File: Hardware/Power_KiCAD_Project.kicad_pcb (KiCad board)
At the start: 4 copper layers, 80 x 93.2 mm, 83 parts, among them J1 Barrel_Jack_MountingPin, J2 XT60 Cell 5, J3 XT60 Cell 4, J4 XT60 Cell 3, J5 XT60 Cell 2, J6 XT60 Cell 1, J7 XT60 To External Switch, J8 L717SDC37P1ACH4F, Q1 PSMN2R6-40YS, Q2 BSS84PH6327XTSA2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

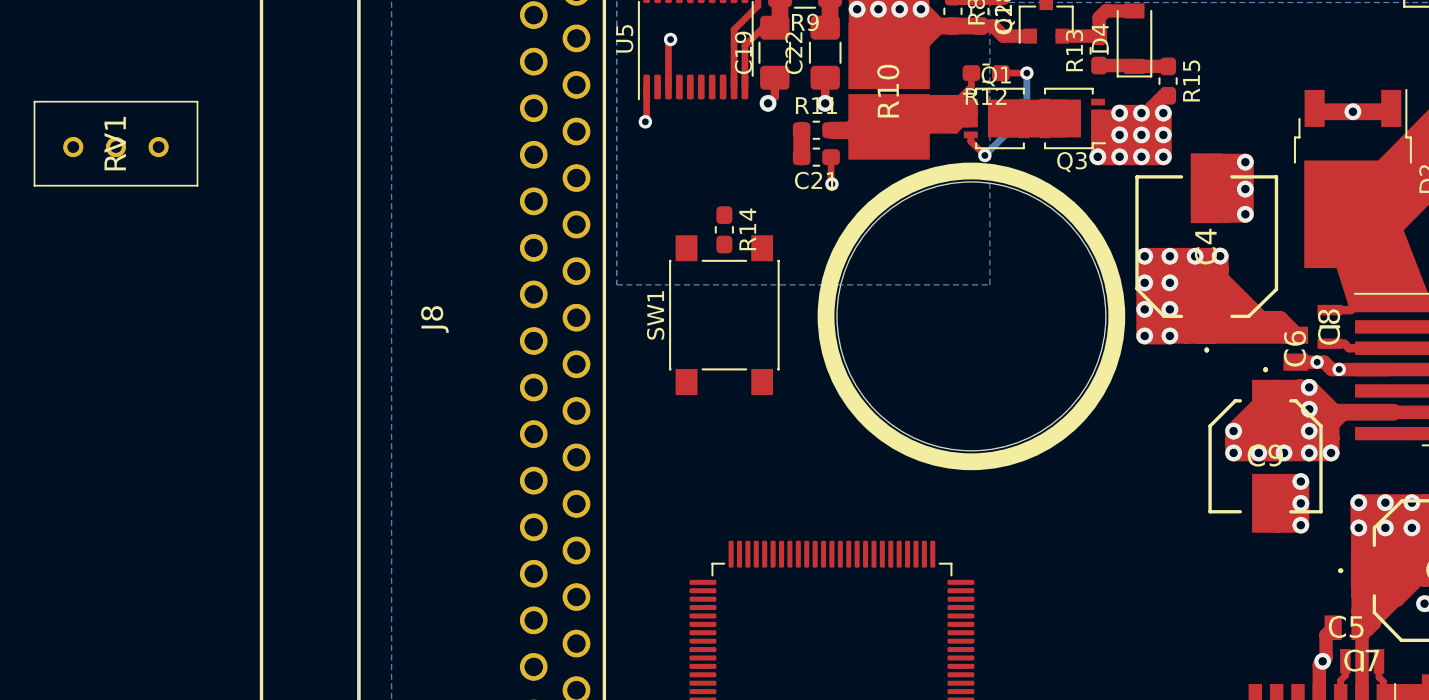
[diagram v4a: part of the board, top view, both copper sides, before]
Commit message: Attempting to add ground vias to help with emi
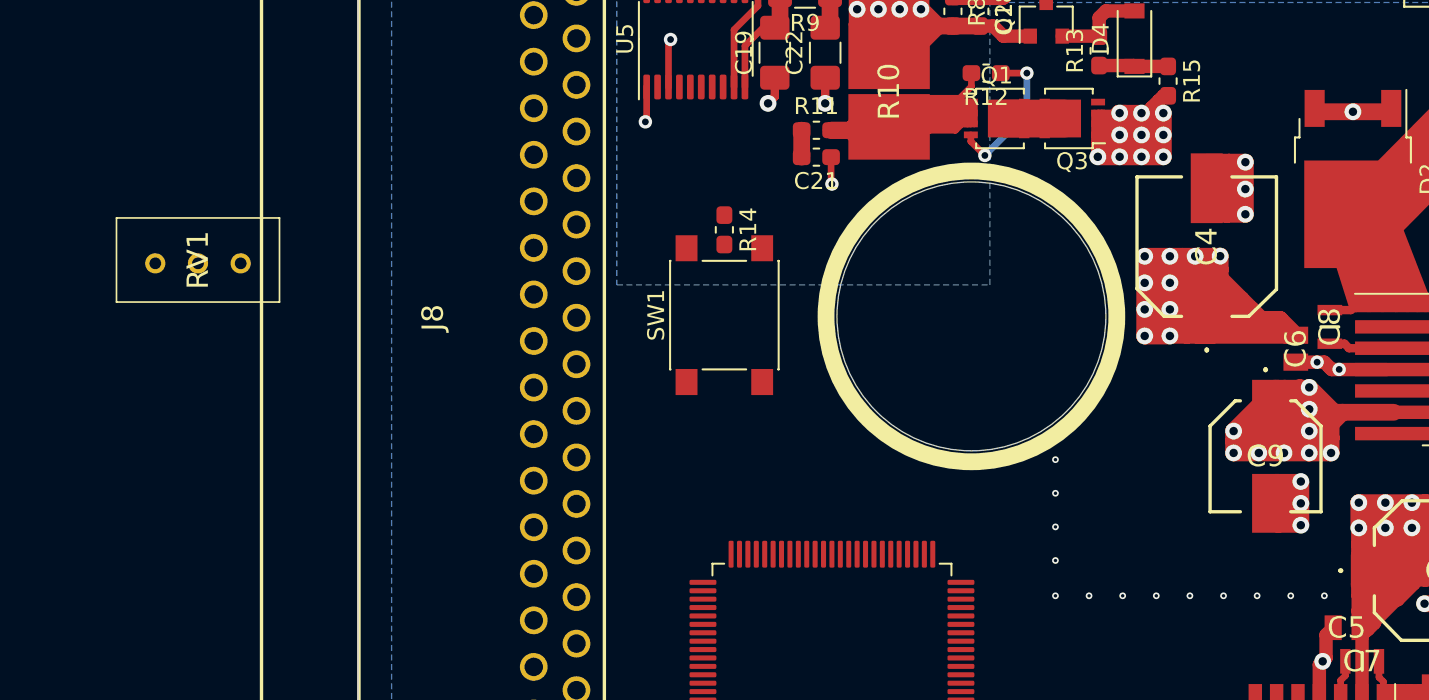
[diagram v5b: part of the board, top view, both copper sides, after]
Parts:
- moved RV1 8.47 mm to (70.5, 95.1)
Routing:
- net GND: vias 27 -> 65
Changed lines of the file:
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@@
     (thickness 1.6)
     (drawings 27)
-    (tracks 794)
+    (tracks 832)
     (zones 0)
     (modules 83)
@@
     (aux_axis_origin 80 145)
     (grid_origin 80 145)
-    (visible_elements 7FFDF77F)
+    (visible_elements 7FFDFF7F)
     (pcbplotparams
       (layerselection 0x010fc_ffffffff)
@@
   )
   (module RDT_Custom_Footprints:T93YA5K10 (layer F.Cu)
-    (at 65.6 88.2 270)
+    (at 70.48 95.12 270)
     (descr T93YA)
     (tags "Variable Resistor")
@@
   (segment (start 148.69 115.57) (end 149.66 114.6) (width 1) (layer F.Cu) (net 2))
   (segment (start 146.56 115.57) (end 148.69 115.57) (width 1) (layer F.Cu) (net 2))
+  (via (at 121.5 115.1) (size 0.4) (drill 0.2) (layers F.Cu B.Cu) (net 2))
+  (via (at 123.5 115.1) (size 0.4) (drill 0.2) (layers F.Cu B.Cu) (net 2))
+  (via (at 125.5 115.1) (size 0.4) (drill 0.2) (layers F.Cu B.Cu) (net 2))
+  (via (at 127.5 115.1) (size 0.4) (drill 0.2) (layers F.Cu B.Cu) (net 2))
+  (via (at 129.5 115.1) (size 0.4) (drill 0.2) (layers F.Cu B.Cu) (net 2))
+  (via (at 131.5 115.1) (size 0.4) (drill 0.2) (layers F.Cu B.Cu) (net 2))
+  (via (at 133.5 115.1) (size 0.4) (drill 0.2) (layers F.Cu B.Cu) (net 2))
+  (via (at 135.5 115.1) (size 0.4) (drill 0.2) (layers F.Cu B.Cu) (net 2))
+  (via (at 137.5 115.1) (size 0.4) (drill 0.2) (layers F.Cu B.Cu) (net 2))
+  (via (at 121.5 113) (size 0.4) (drill 0.2) (layers F.Cu B.Cu) (net 2))
+  (via (at 121.5 111) (size 0.4) (drill 0.2) (layers F.Cu B.Cu) (net 2))
+  (via (at 121.5 109) (size 0.4) (drill 0.2) (layers F.Cu B.Cu) (net 2))
+  (via (at 121.5 107) (size 0.4) (drill 0.2) (layers F.Cu B.Cu) (net 2))
+  (via (at 116.5 107.22) (size 0.4) (drill 0.2) (layers F.Cu B.Cu) (net 2))
+  (via (at 118.67355 106.945417) (size 0.4) (drill 0.2) (layers F.Cu B.Cu) (net 2))
+  (via (at 120.710527 106.13892) (size 0.4) (drill 0.2) (layers F.Cu B.Cu) (net 2))
+  (via (at 122.482942 104.851186) (size 0.4) (drill 0.2) (layers F.Cu B.Cu) (net 2))
+  (via (at 123.879426 103.163126) (size 0.4) (drill 0.2) (layers F.Cu B.Cu) (net 2))
+  (via (at 124.812234 101.180809) (size 0.4) (drill 0.2) (layers F.Cu B.Cu) (net 2))
+  (via (at 125.222754 99.028789) (size 0.4) (drill 0.2) (layers F.Cu B.Cu) (net 2))
+  (via (at 125.085191 96.842287) (size 0.4) (drill 0.2) (layers F.Cu B.Cu) (net 2))
+  (via (at 124.408188 94.758689) (size 0.4) (drill 0.2) (layers F.Cu B.Cu) (net 2))
+  (via (at 123.234286 92.908914) (size 0.4) (drill 0.2) (layers F.Cu B.Cu) (net 2))
+  (via (at 121.637243 91.409191) (size 0.4) (drill 0.2) (layers F.Cu B.Cu) (net 2))
+  (via (at 119.717409 90.353754) (size 0.4) (drill 0.2) (layers F.Cu B.Cu) (net 2))
+  (via (at 117.595412 89.808918) (size 0.4) (drill 0.2) (layers F.Cu B.Cu) (net 2))
+  (via (at 115.404588 89.808918) (size 0.4) (drill 0.2) (layers F.Cu B.Cu) (net 2))
+  (via (at 113.282591 90.353754) (size 0.4) (drill 0.2) (layers F.Cu B.Cu) (net 2))
+  (via (at 111.362757 91.409191) (size 0.4) (drill 0.2) (layers F.Cu B.Cu) (net 2))
+  (via (at 109.765714 92.908914) (size 0.4) (drill 0.2) (layers F.Cu B.Cu) (net 2))
+  (via (at 108.591812 94.758689) (size 0.4) (drill 0.2) (layers F.Cu B.Cu) (net 2))
+  (via (at 107.914809 96.842287) (size 0.4) (drill 0.2) (layers F.Cu B.Cu) (net 2))
+  (via (at 107.777246 99.028789) (size 0.4) (drill 0.2) (layers F.Cu B.Cu) (net 2))
+  (via (at 108.187766 101.180809) (size 0.4) (drill 0.2) (layers F.Cu B.Cu) (net 2))
+  (via (at 109.120574 103.163126) (size 0.4) (drill 0.2) (layers F.Cu B.Cu) (net 2))
+  (via (at 110.517058 104.851186) (size 0.4) (drill 0.2) (layers F.Cu B.Cu) (net 2))
+  (via (at 112.289473 106.13892) (size 0.4) (drill 0.2) (layers F.Cu B.Cu) (net 2))
+  (via (at 114.32645 106.945417) (size 0.4) (drill 0.2) (layers F.Cu B.Cu) (net 2))
   (segment (start 134.42 103.58) (end 134 104) (width 0.8) (layer F.Cu) (net 3))
   (segment (start 136.12 103.98) (end 136.1 104) (width 0.8) (layer F.Cu) (net 3))
@@
     (polygon
       (pts
-        (xy 158 126.5) (xy 94.7 126.45) (xy 94.7 103.3) (xy 121 103.3) (xy 121 115.6)
+        (xy 158 126.5) (xy 94.7 126.45) (xy 94.7 103.5) (xy 121 103.5) (xy 121 115.6)
         (xy 146.9 115.6) (xy 146.9 108) (xy 131.3 108) (xy 131.3 104.1) (xy 132.6 104.1)
         (xy 132.6 102.1) (xy 143.8 102) (xy 143.8 88.5) (xy 158 88.5)

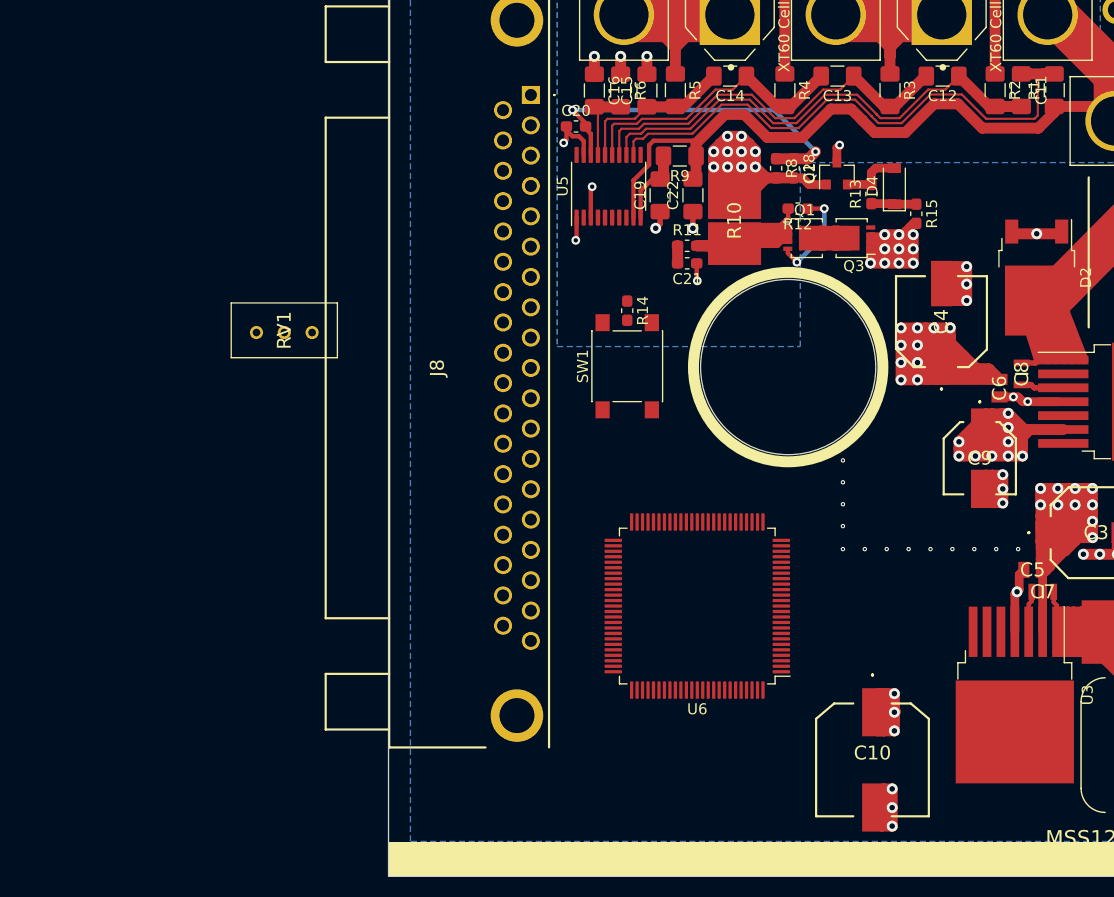
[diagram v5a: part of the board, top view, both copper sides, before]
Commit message: More adjustments of internal planes
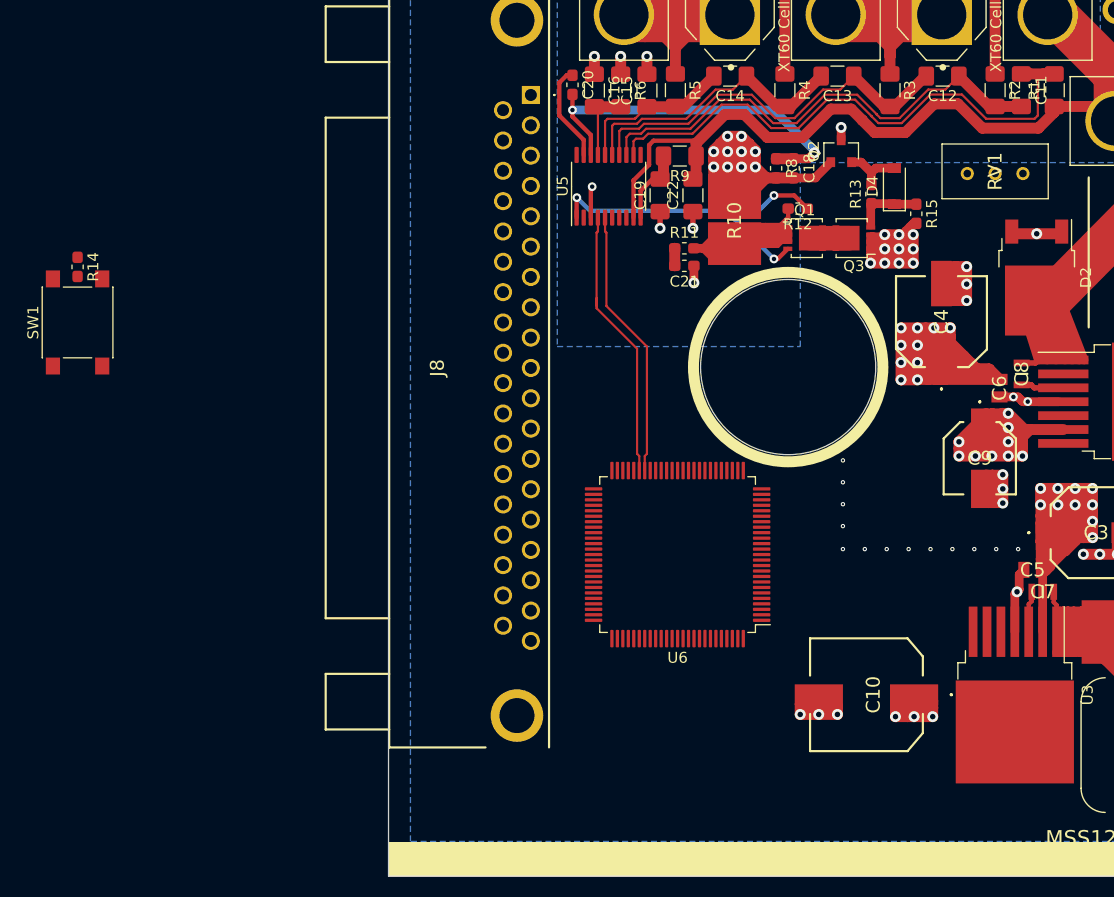
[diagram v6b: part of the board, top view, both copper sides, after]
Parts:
- moved RV1 66.5 mm to (135.4, 80.6)
- moved R14 50.4 mm to (51.6, 89.3)
- moved SW1 50.4 mm to (51.6, 94.4)
- moved C10 5.98 mm to (123.7, 128.4), turned to 90 degrees
- moved U6 5.03 mm to (106.4, 115.6)
- moved C20 3.81 mm to (96.8, 72.7), turned to 270 degrees
- moved Q2 2.08 mm to (121.3, 78.8)
- moved R11 0.35 mm to (107.0, 87.6)
- moved C21 0.35 mm to (107.0, 89.2)
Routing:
- net /I2C_SDA: track 0.00 -> 25.5 mm
- net /I2C_SCL: track 0.00 -> 24.8 mm
- net Net-(Q1-Pad4): track 11.2 -> 32.4 mm
- net Net-(C20-Pad1): track 6.81 -> 10.6 mm, vias 1 -> 0
- net Net-(Q1-Pad1): track 43.0 -> 40.0 mm
- net Net-(D4-Pad1): track 4.12 -> 6.10 mm
- net Net-(C18-Pad1): track 32.4 -> 33.8 mm
- net GNDREF: track 211.8 -> 212.4 mm
- net Net-(Q2-Pad3): track 1.70 -> 1.17 mm
- added copper zone on 3.3V.Cu, net +5V

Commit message: Routed all connections and placed all components
MCU crystal still needs a ground peninsula
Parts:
- C23: footprint Capacitor_SMD:C_1206_3216Metric_Pad1.42x1.75mm_HandSolder -> Capacitor_SMD:C_0603_1608Metric_Pad1.08x0.95mm_HandSolder
- moved C31 213.9 mm to (96.7, 122.6), turned to 90 degrees
- moved C27 206.7 mm to (97.8, 128.2), turned to 270 degrees
- moved C28 205.0 mm to (97.9, 111.0), turned to 90 degrees
- moved C36 201.9 mm to (117.9, 117.7), turned to 270 degrees
- moved R19 200.7 mm to (107.2, 129.9), turned to 180 degrees
- moved C34 199.2 mm to (101.5, 108.7), turned to 90 degrees
- moved R18 198.4 mm to (102.6, 129.9)
- moved C33 195.3 mm to (111.4, 130.6), turned to 270 degrees
- moved C32 191.5 mm to (116.4, 122.2), turned to 270 degrees
- moved C24 189.9 mm to (119.4, 121.6), turned to 270 degrees
- moved C30 187.0 mm to (116.4, 125.6), turned to 270 degrees
- moved C26 186.9 mm to (114.3, 129.6)
- moved R16 186.3 mm to (121.8, 113.5), turned to 270 degrees
- moved C29 185.3 mm to (115.5, 110.9)
- moved C35 184.4 mm to (116.4, 115.6), turned to 270 degrees
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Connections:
- R18 pad 1: /DSUB-37_Bus/Alert_scl -> /I2C_SCL
- R19 pad 1: /DSUB-37_Bus/Alert_sda -> /I2C_SDA
- U6 pad 30: Net-(U6-Pad30) -> Net-(D6-Pad2)
- U6 pad 31: Net-(U6-Pad31) -> Net-(D5-Pad2)
- U6 pad 32: Net-(U6-Pad32) -> /TEMP_ALERT_1
- U6 pad 34: Net-(U6-Pad34) -> /BATT_ALERT
- U6 pad 35: /BATT_ALERT -> Net-(U6-Pad35)
- U6 pad 36: /TEMP_ALERT_1 -> Net-(U6-Pad36)
- U6 pad 37: /TEMP_ALERT_2 -> /STM32L562VET6Q 1/ABORT_1
- U6 pad 38: Net-(D5-Pad2) -> /TEMP_ALERT_2
- U6 pad 39: Net-(D6-Pad2) -> Net-(U6-Pad39)
- U6 pad 40: Net-(U6-Pad40) -> /STM32L562VET6Q 1/ABORT_2
- U6 pad 42: /STM32L562VET6Q 1/ABORT_1 -> Net-(U6-Pad42)
- U6 pad 43: /STM32L562VET6Q 1/ABORT_2 -> Net-(U6-Pad43)
- U6 pad 44: /I2C_SCL -> /DSUB-37_Bus/Alert_scl
- U6 pad 45: /I2C_SDA -> /DSUB-37_Bus/Alert_sda
- U6 pad 52: Net-(U6-Pad52) -> /DSUB-37_Bus/Alert_Active
- U6 pad 91: /DSUB-37_Bus/Alert_Active -> /STM32L562VET6Q 1/I2C1_EN
- U6 pad 92: /DSUB-37_Bus/Alert_scl -> /I2C_SCL
- U6 pad 93: /DSUB-37_Bus/Alert_sda -> /I2C_SDA
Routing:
- net +5V: track 15.1 -> 156.6 mm, vias 3 -> 12
- net /I2C_SCL: track 24.8 -> 143.4 mm, vias 0 -> 4
- net /I2C_SDA: track 25.5 -> 139.0 mm, vias 0 -> 6
- net GND: track 102.9 -> 173.1 mm, vias 65 -> 130
- net +3V3: track 87.0 -> 156.4 mm, vias 19 -> 34
- net Net-(R14-Pad1): track 0.00 -> 65.1 mm, vias 0 -> 3
- net /STM32L562VET6Q 1/DEBUG_SWDIO: track 0.00 -> 60.6 mm, vias 0 -> 2
- net /STM32L562VET6Q 1/DEBUG_SWCLK: track 0.00 -> 58.3 mm, vias 0 -> 2
- net /TEMP_ALERT_1: track 0.00 -> 52.0 mm, vias 0 -> 2
- net /DSUB-37_Bus/NRST: track 0.00 -> 51.1 mm, vias 0 -> 1
- net /BATT_ALERT: track 0.00 -> 42.7 mm, vias 0 -> 2
- net /DSUB-37_Bus/Alert_sda: track 0.00 -> 36.3 mm
- net /DSUB-37_Bus/Alert_scl: track 0.00 -> 35.1 mm
- net /LiPo Pack Monitor/VC1: track 14.8 -> 49.0 mm, vias 0 -> 2
- net Net-(Q2-Pad3): track 1.17 -> 31.2 mm, vias 1 -> 2
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- added copper zone on F.Cu, net GND
- added copper zone on B.Cu, net GNDREF
- added copper zone on F.Cu, net GNDREF

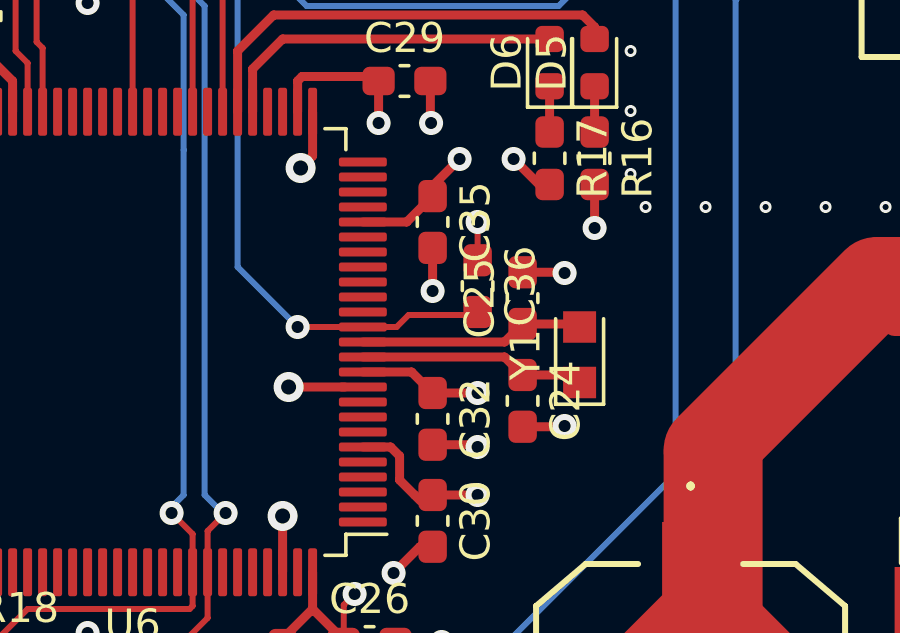
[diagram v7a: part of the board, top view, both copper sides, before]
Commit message: Added ground peninsula for MCU crystal
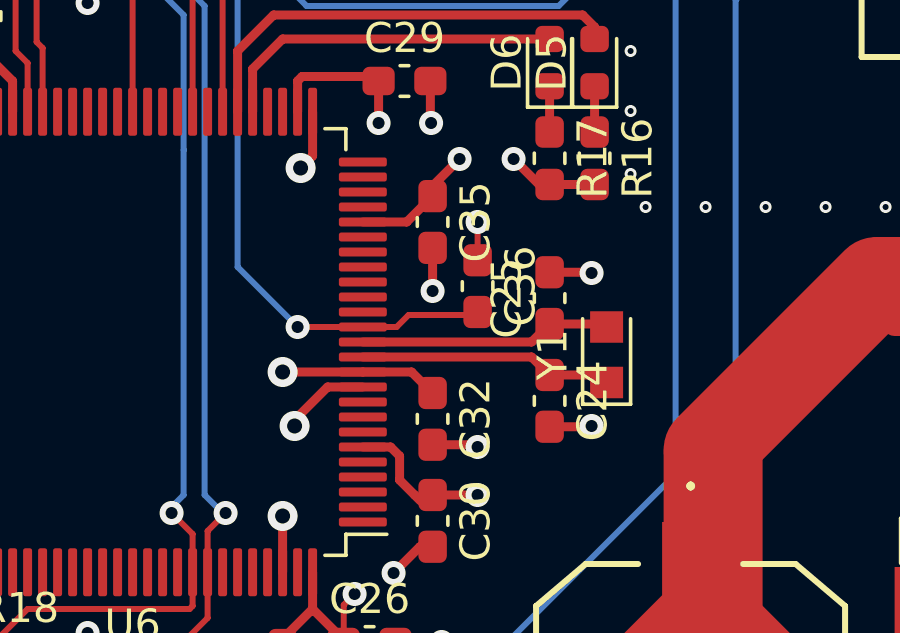
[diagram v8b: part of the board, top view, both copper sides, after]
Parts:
- moved Y1 0.90 mm to (122.2, 120.0)
- moved C24 0.90 mm to (120.3, 121.6)
- moved C25 0.90 mm to (120.3, 118.1)
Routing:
- net +3V3: track 156.4 -> 157.6 mm
- net GND: track 173.1 -> 174.2 mm, vias 130 -> 129
- net Net-(C24-Pad1): track 7.58 -> 8.48 mm
- net Net-(C25-Pad1): track 7.51 -> 8.41 mm
